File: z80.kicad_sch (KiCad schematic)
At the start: 39 parts, among them IC4 Z80CPU, IC5 64k_SRAM_Z80, IC901 TL974

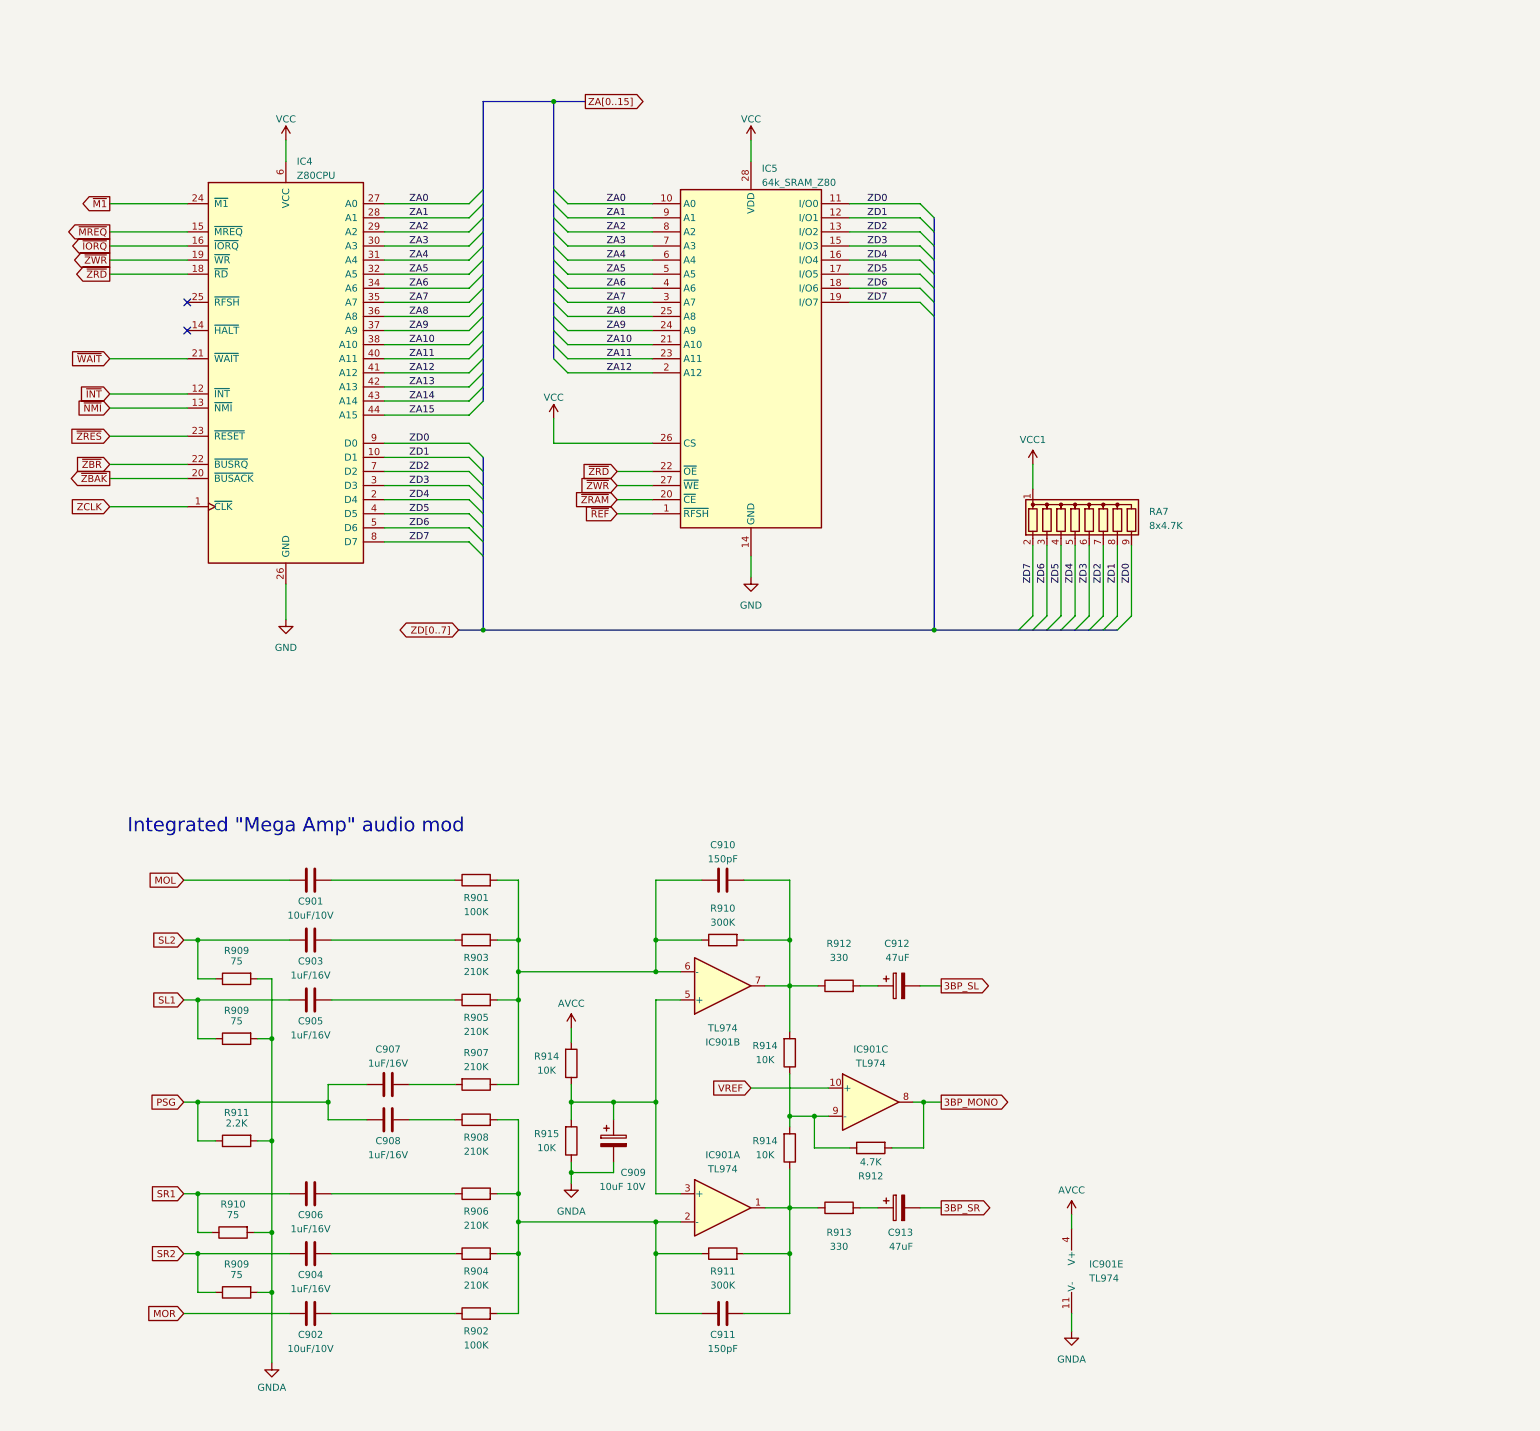
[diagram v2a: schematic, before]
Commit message: Use PAC-10 as example for missing VREF, make mono op-amp non-inverting to match stereo audio polarity.
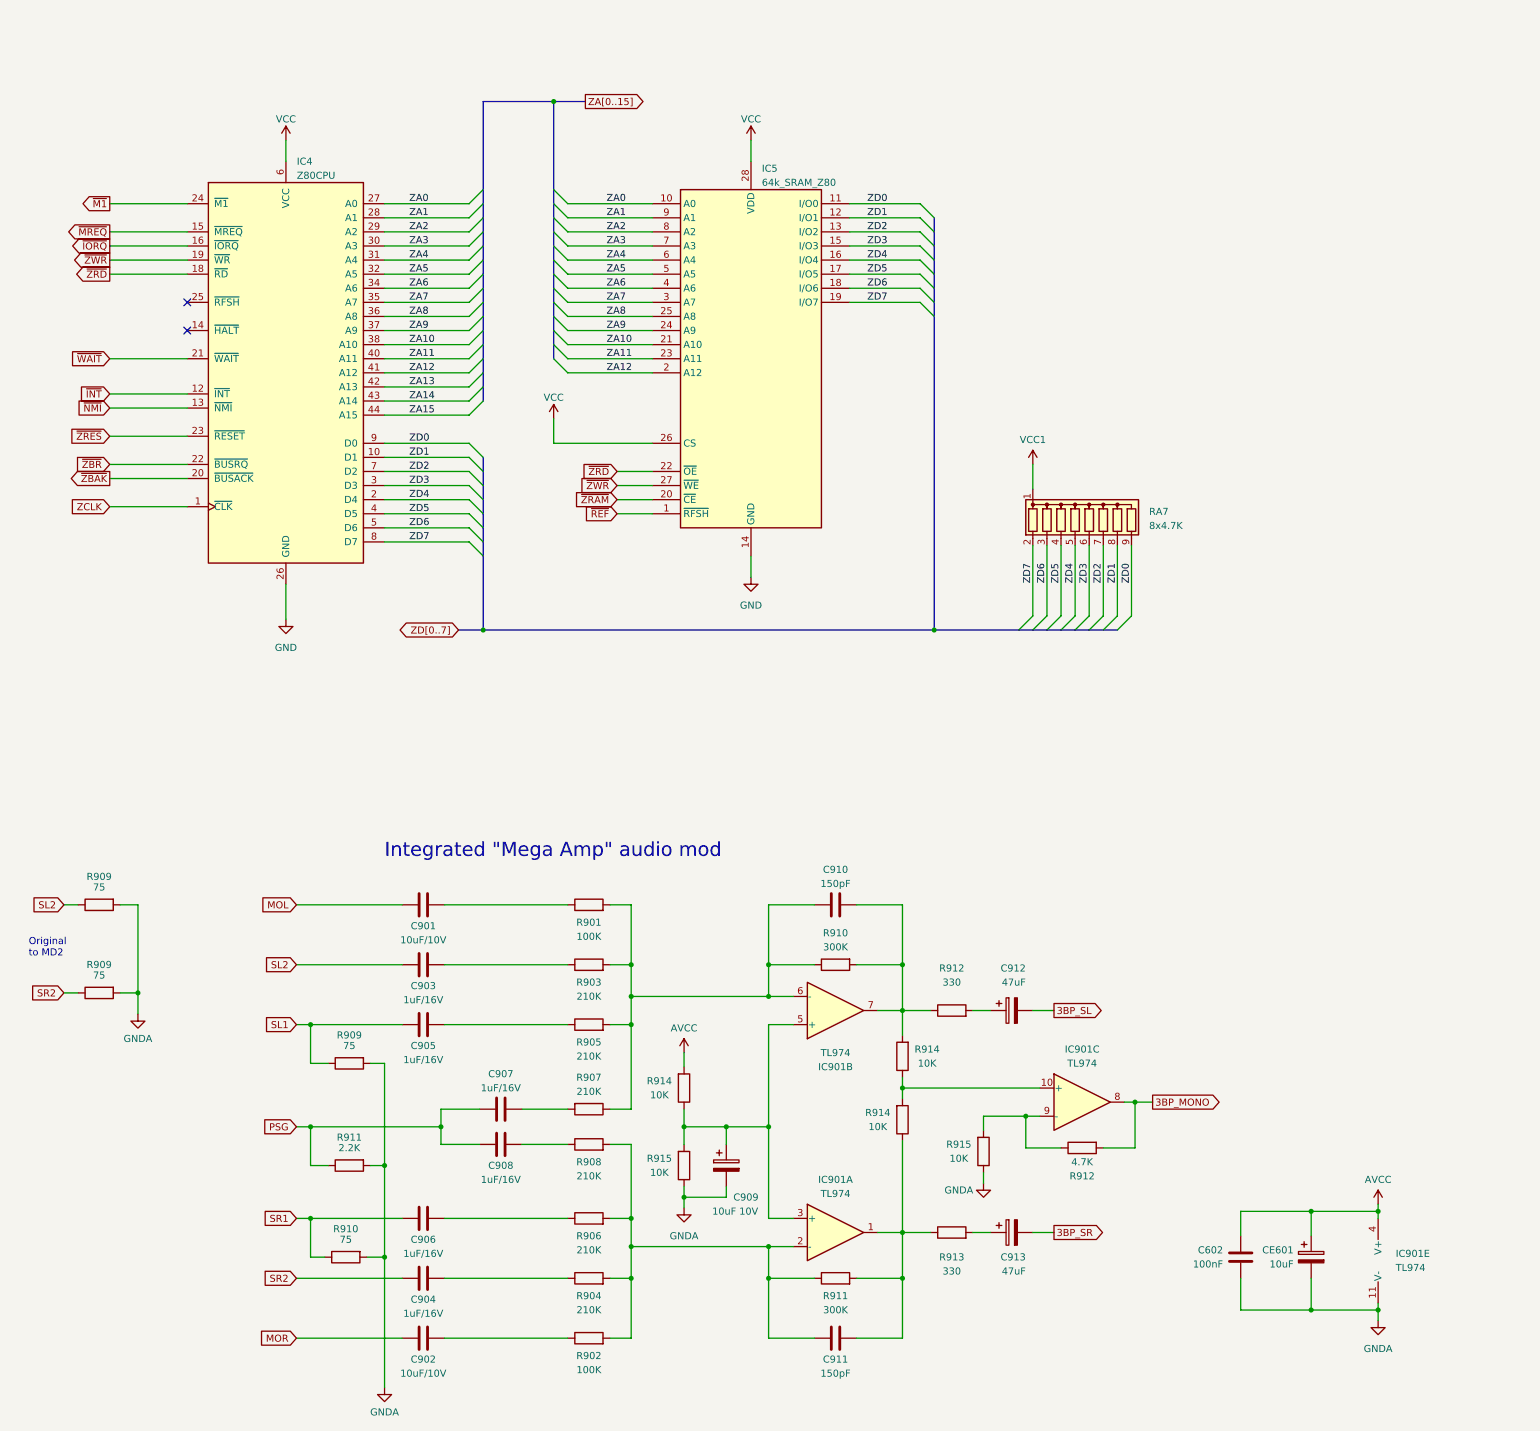
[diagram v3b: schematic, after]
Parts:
- added C602: 100nF, symbol Device:C
- added CE601: 10uF, symbol Device:C_Polarized
- added R915: 10K, symbol Device:R
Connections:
- net VREF is gone; now on an unnamed net: IC901.10 (+)
- net AVCC: now also C602.1, CE601.1
- net GNDA: now also C602.2, CE601.2, R915.1
- net at R914.1, R914.2: no longer IC901.9 (-), R912.1
- new net: IC901.9 (-), R912.1, R915.2
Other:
- note added: "Original to MD2"
- moved on the sheet: C901, C902, C903, C904, C905, C906, C907, C908, C909, C910, C911, C912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

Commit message: Start PCB layout.
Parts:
- C602, C901, C902, C903, C904, C905, C906, C907, C908, C909, C910, C911, C912, C913: footprint (none) -> Capacitor_SMD:C_0805_2012Metric
- IC5: value 64k_SRAM_Z80 -> LC3664
- R901, R902, R903, R904, R905, R906, R907, R908, R909, R910, R911, R912, R913, R914, R915: footprint (none) -> Resistor_SMD:R_0805_2012Metric

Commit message: Save first mock-up before updating footprints.
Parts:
- IC5: footprint Package_SO:SSOP-28_3.9x9.9mm_P0.635mm -> Package_SO:SOIC-28W_7.5x18.7mm_P1.27mm
- IC901: footprint (none) -> Package_SO:SO-14_3.9x8.65mm_P1.27mm
- RA7: footprint (none) -> Neptune:RA_8_Common
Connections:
- net 3BP_MONO renamed MA_MONO
- net 3BP_SL renamed MA_SL
- net 3BP_SR renamed MA_SR
- net SL1 renamed SL4
- net SR1 renamed SR4
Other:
- note added: "Audio Signals MOL/MOR: MD2 FM (ASIC) SL1/SR1: Cartridge audio* SL2/SR2: Expansion IN (e.g. Mega CD) SL3/SR3: Expansion OUT (not connected) SL4/SR4: 32X PCM + Cartridge audio * Not used as this is mixed into SL4/SR4 by IC511."
- moved on the sheet: C602, C901, C902, C903, C904, C905, C906, C907, C908, C909, C910, C911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

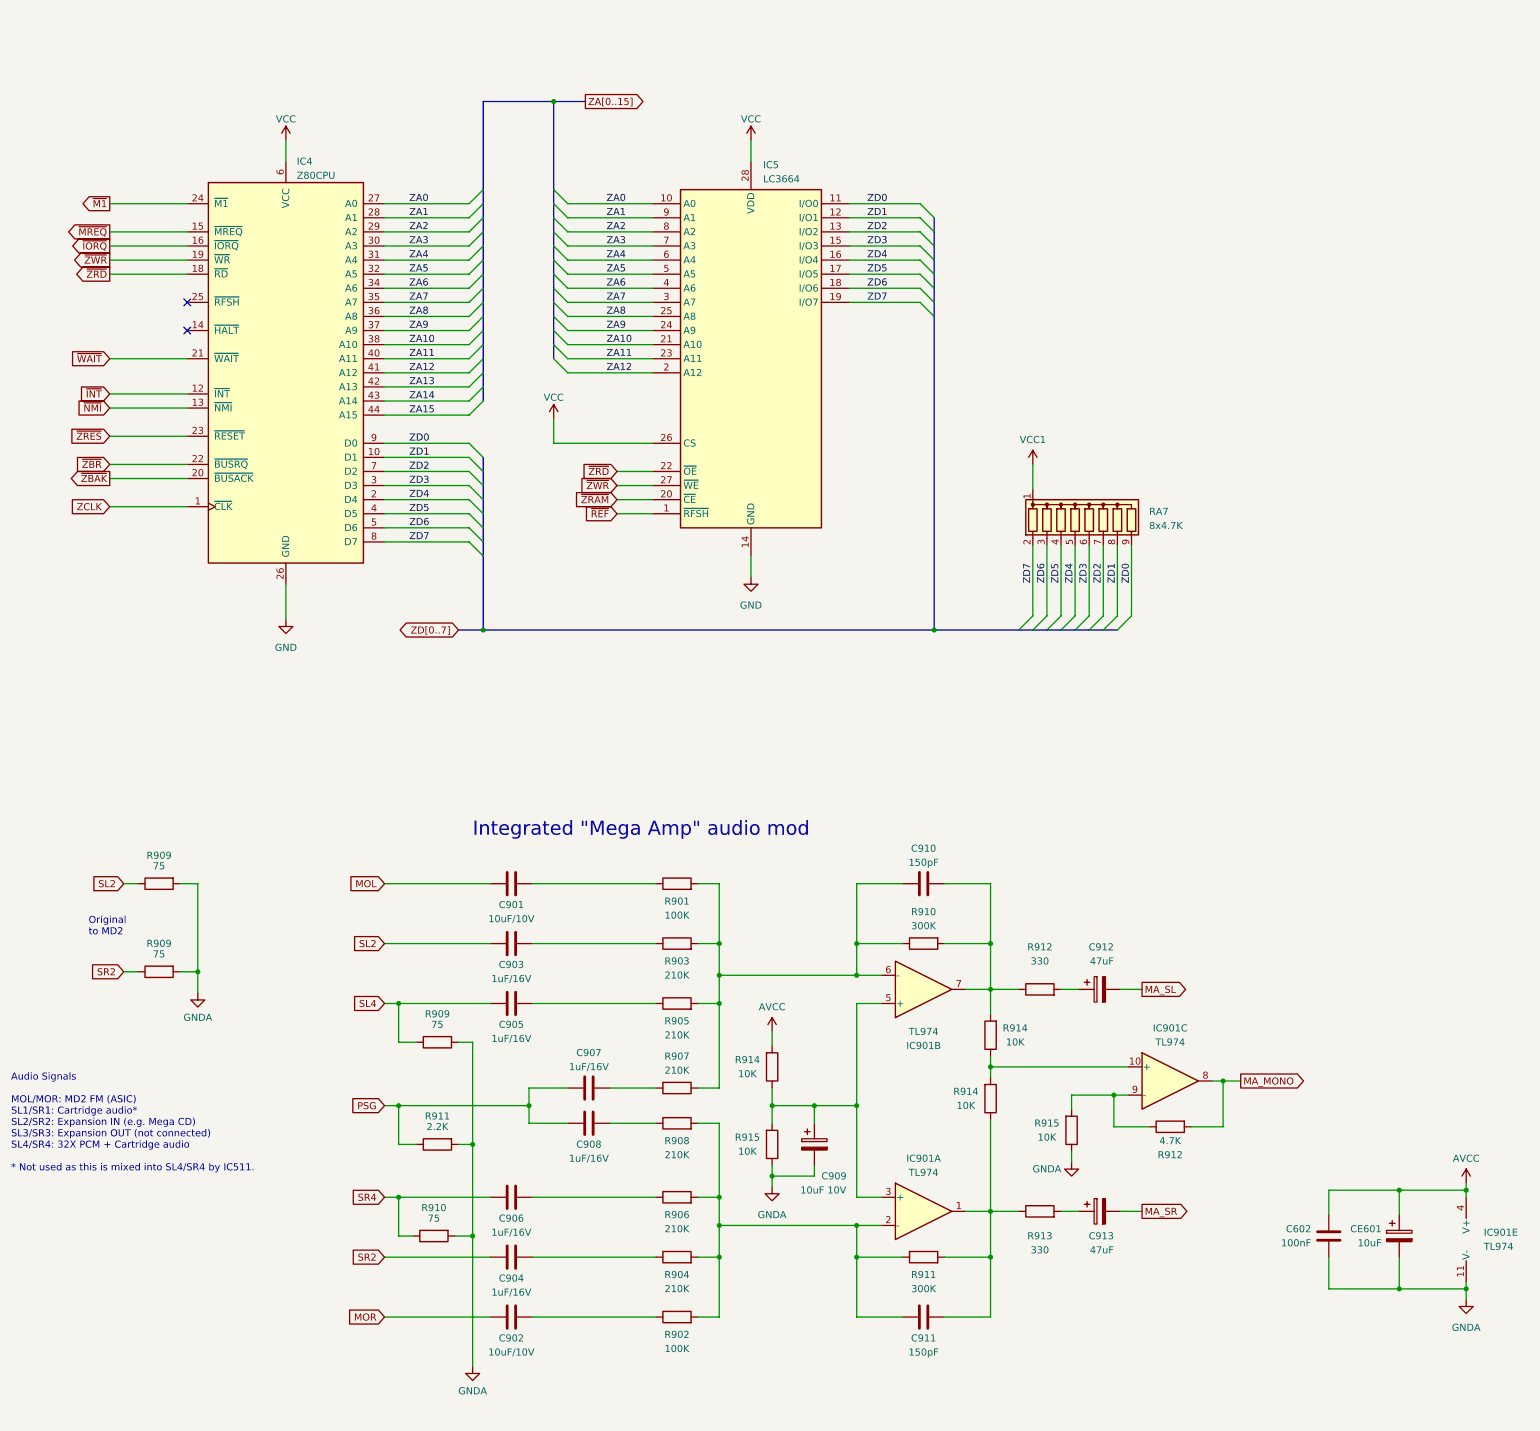
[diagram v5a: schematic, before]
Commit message: Draft new layout with more accurate footprints.
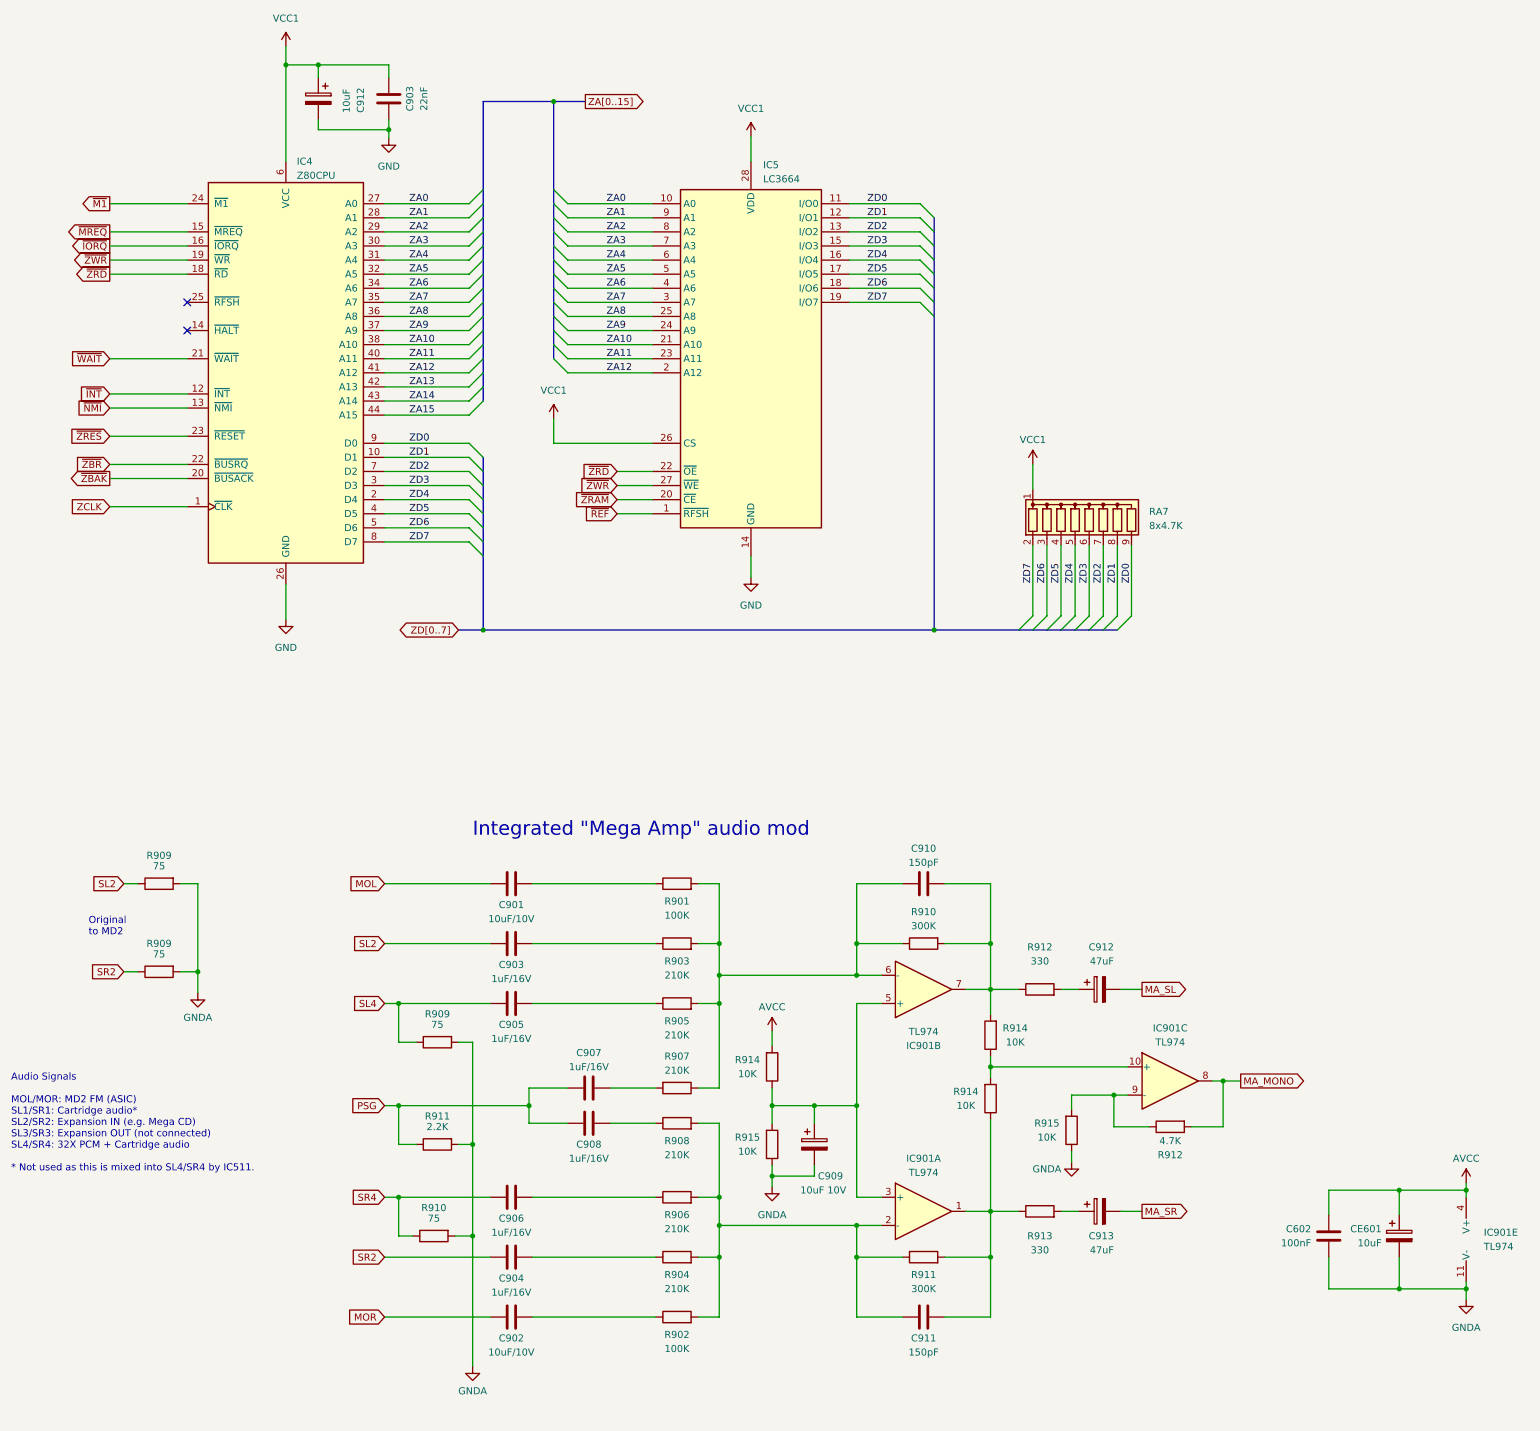
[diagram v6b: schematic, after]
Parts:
- added C903: 22nF, Capacitor_SMD:C_0805_2012Metric, symbol Device:C
- added C912: 10uF, Capacitor_THT:CP_Radial_D5.0mm_P2.50mm, symbol Device:C_Polarized
- C909, C912, C913: footprint Capacitor_SMD:C_0805_2012Metric -> Capacitor_THT:CP_Radial_D5.0mm_P2.50mm
- CE601: footprint (none) -> Capacitor_THT:CP_Radial_D5.0mm_P2.50mm
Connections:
- net VCC is gone; now on net VCC1: IC4.6 (VCC), IC5.26 (CS), IC5.28 (VDD)
- net GND: now also C903.1, C912.2
- net VCC1: now also C903.2, C912.1
